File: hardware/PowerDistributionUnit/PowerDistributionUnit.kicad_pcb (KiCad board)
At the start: 2 copper layers, 99.1 x 60.2 mm, 100 parts, among them J1 973582101, J2 973582100, J3 973582101, J4 973582100, Q1 SQJ141ELP, Q2 CSD18511Q5A, SW1 SW_Push, U1 TPS25983, U2 AD5258, U3 NUCLEO_L432KC

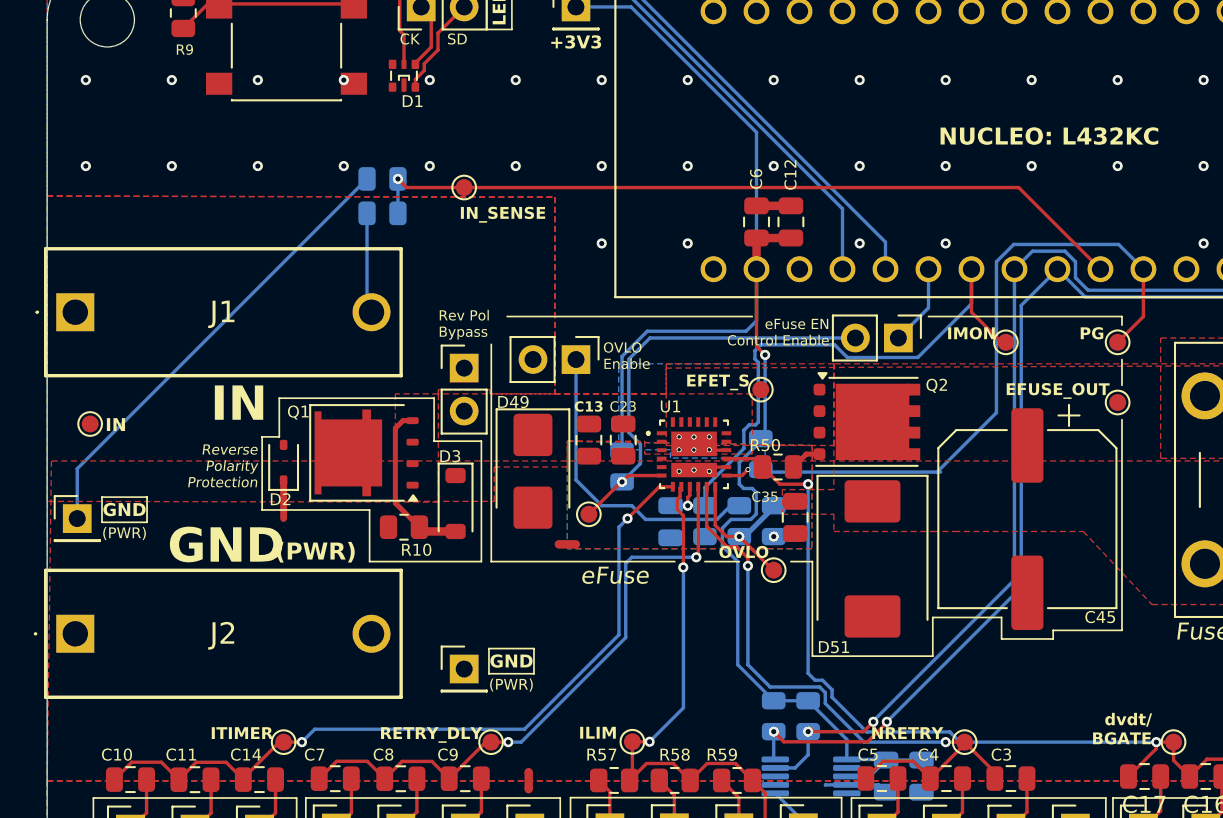
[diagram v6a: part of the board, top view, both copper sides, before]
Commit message: Changed a gnd pwr tp to gnd. Reduced capacitor value at output. Changed pwr gnd to gnd for input resistor divider.
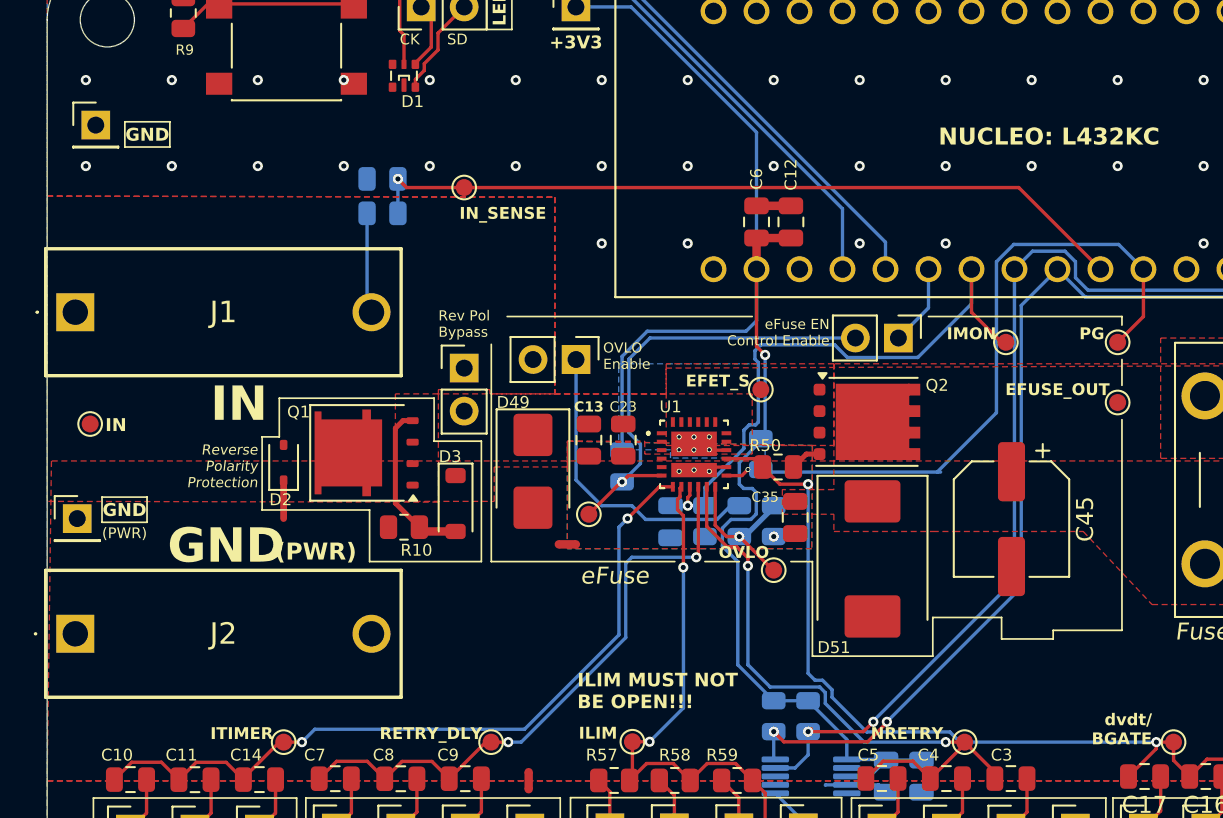
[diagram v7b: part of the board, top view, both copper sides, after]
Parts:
- C45: value 220u -> 100u; footprint Capacitor_SMD:CP_Elec_10x12.6 -> Capacitor_SMD:CP_Elec_6.3x9.9
- moved TP14 38.8 mm to (93.7, 80.5)
- moved C45 0.94 mm to (147.8, 103.8)
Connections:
- R8 pad 2: GNDPWR -> GND
- TP14 pad 1: GNDPWR -> GND
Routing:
- net GNDPWR: track 29.4 -> 2.25 mm
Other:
- board text added: "ILIM MUST NOT BE OPEN!!!"
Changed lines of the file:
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@@
 	(footprint "Connector_PinHeader_2.54mm:PinHeader_1x01_P2.54mm_Vertical"
 		(layer "F.Cu")
-		(at 115.492 112.656)
+		(at 93.726 80.518)
 		(descr "Through hole straight pin header, 1x01, 2.54mm pitch, single row")
 		(tags "Through hole pin header THT 1x01 2.54mm single row")
@@
 			(layers "*.Cu" "*.Mask")
 			(remove_unused_layers no)
-			(net 18 "GNDPWR")
+			(net 1 "GND")
 			(pinfunction "1")
 			(pintype "passive")
@@
 		)
 	)
-	(footprint "Capacitor_SMD:CP_Elec_10x12.6"
+	(footprint "Capacitor_SMD:CP_Elec_6.3x9.9"
 		(layer "F.Cu")
-		(at 148.766 103.798 -90)
-		(descr "SMD capacitor, aluminum electrolytic, Panasonic F12, 10.0x12.6mm")
+		(at 147.828 103.798 -90)
+		(descr "SMD capacitor, aluminum electrolytic, Panasonic C10, 6.3x9.9mm")
 		(tags "capacitor electrolytic")
 		(property "Reference" "C45"
-			(at 5.81 -4.318 180)
+			(at 0 -4.35 -90)
 			(layer "F.SilkS")
 			(effects
 				(font
-					(size 0.7 0.7)
-					(thickness 0.1)
+					(size 1 1)
+					(thickness 0.15)
 				)
 			)
 		)
-		(property "Value" "220u"
-			(at 0 6.2 90)
+		(property "Value" "100u"
+			(at 0 4.35 -90)
 			(layer "F.Fab")
 			(effects
@@
 			)
 		)
-		(property "Footprint" "Capacitor_SMD:CP_Elec_10x12.6"
+		(property "Footprint" "Capacitor_SMD:CP_Elec_6.3x9.9"
 			(at 0 0 -90)
 			(unlocked yes)
@@
 		(attr smd)
 		(fp_line
-			(start -4.195563 5.26)
-			(end 5.26 5.26)
+			(start -2.345563 3.41)
+			(end 3.41 3.41)
 			(stroke
 				(width 0.12)
@@
 		)
 		(fp_line
-			(start 5.26 5.26)
-			(end 5.26 1.21)
+			(start 3.41 3.41)
+			(end 3.41 1.06)
 			(stroke
 				(width 0.12)
@@
 		)
 		(fp_line
-			(start -5.26 4.195563)
-			(end -4.195563 5.26)
+			(start -3.41 2.345563)
+			(end -2.345563 3.41)
 			(stroke
 				(width 0.12)
@@
 		)
 		(fp_line
-			(start -5.26 4.195563)
-			(end -5.26 1.21)
+			(start -3.41 2.345563)
+			(end -3.41 1.06)
 			(stroke
 				(width 0.12)
@@
 		)
 		(fp_line
-			(start -6.75 -2.46)
-			(end -5.5 -2.46)
+			(start -4.4375 -1.8475)
+			(end -3.65 -1.8475)
 			(stroke
 				(width 0.12)
@@
 		)
 		(fp_line
-			(start -6.125 -3.085)
-			(end -6.125 -1.835)
+			(start -4.04375 -2.24125)
+			(end -4.04375 -1.45375)
 			(stroke
 				(width 0.12)
@@
 		)
 		(fp_line
-			(start -5.26 -4.195563)
-			(end -5.26 -1.21)
+			(start -3.41 -2.345563)
+			(end -3.41 -1.06)
 			(stroke
 				(width 0.12)
@@
 		)
 		(fp_line
-			(start -5.26 -4.195563)
-			(end -4.195563 -5.26)
+			(start -3.41 -2.345563)
+			(end -2.345563 -3.41)
 			(stroke
 				(width 0.12)
@@
 		)
 		(fp_line
-			(start -4.195563 -5.26)
-			(end 5.26 -5.26)
+			(start -2.345563 -3.41)
+			(end 3.41 -3.41)
 			(stroke
 				(width 0.12)
@@
 		)
 		(fp_line
-			(start 5.26 -5.26)
-			(end 5.26 -1.21)
+			(start 3.41 -3.41)
+			(end 3.41 -1.06)
 			(stroke
 				(width 0.12)
@@
 		)
 		(fp_line
-			(start -4.25 5.4)
-			(end 5.4 5.4)
+			(start -2.4 3.55)
+			(end 3.55 3.55)
 			(stroke
 				(width 0.05)
@@
 		)
 		(fp_line
-			(start -5.4 4.25)
-			(end -4.25 5.4)
+			(start -3.55 2.4)
+			(end -2.4 3.55)
 			(stroke
 				(width 0.05)
@@
 		)
 		(fp_line
-			(start -6.8 1.2)
-			(end -5.4 1.2)
+			(start -4.8 1.05)
+			(end -3.55 1.05)
 			(stroke
 				(width 0.05)
@@
 		)
 		(fp_line
-			(start -5.4 1.2)
-			(end -5.4 4.25)
+			(start -3.55 1.05)
+			(end -3.55 2.4)
 			(stroke
 				(width 0.05)
@@
 		)
 		(fp_line
-			(start 5.4 1.2)
-			(end 5.4 5.4)
+			(start 3.55 1.05)
+			(end 3.55 3.55)
 			(stroke
 				(width 0.05)
@@
 		)
 		(fp_line
-			(start 6.8 1.2)
-			(end 5.4 1.2)
+			(start 4.8 1.05)
+			(end 3.55 1.05)
 			(stroke
 				(width 0.05)
@@
 		)
 		(fp_line
-			(start -6.8 -1.2)
-			(end -6.8 1.2)
+			(start -4.8 -1.05)
+			(end -4.8 1.05)
 			(stroke
 				(width 0.05)
@@
 		)
 		(fp_line
-			(start -5.4 -1.2)
-			(end -6.8 -1.2)
+			(start -3.55 -1.05)
+			(end -4.8 -1.05)
 			(stroke
 				(width 0.05)
@@
 		)
 		(fp_line
-			(start 5.4 -1.2)
-			(end 6.8 -1.2)
+			(start 3.55 -1.05)
+			(end 4.8 -1.05)
 			(stroke
 				(width 0.05)
@@
 		)
 		(fp_line
-			(start 6.8 -1.2)
-			(end 6.8 1.2)
+			(start 4.8 -1.05)
+			(end 4.8 1.05)
 			(stroke
 				(width 0.05)
@@
 		)
 		(fp_line
-			(start -5.4 -4.25)
-			(end -5.4 -1.2)
+			(start -3.55 -2.4)
+			(end -3.55 -1.05)
 			(stroke
 				(width 0.05)
@@
 		)
 		(fp_line
-			(start -5.4 -4.25)
-			(end -4.25 -5.4)
+			(start -3.55 -2.4)
+			(end -2.4 -3.55)
 			(stroke
 				(width 0.05)
@@
 		)
 		(fp_line
-			(start -4.25 -5.4)
-			(end 5.4 -5.4)
+			(start -2.4 -3.55)
+			(end 3.55 -3.55)
 			(stroke
 				(width 0.05)
@@
 		)
 		(fp_line
-			(start 5.4 -5.4)
-			(end 5.4 -1.2)
+			(start 3.55 -3.55)
+			(end 3.55 -1.05)
 			(stroke
 				(width 0.05)
@@
 		)
 		(fp_line
-			(start -4.15 5.15)
-			(end 5.15 5.15)
+			(start -2.3 3.3)
+			(end 3.3 3.3)
 			(stroke
 				(width 0.1)
@@
 		)
 		(fp_line
-			(start -5.15 4.15)
-			(end -4.15 5.15)
+			(start -3.3 2.3)
+			(end -2.3 3.3)
 			(stroke
 				(width 0.1)
@@
 		)
 		(fp_line
-			(start -4.558325 -1.7)
-			(end -3.558325 -1.7)
+			(start -2.704838 -1.33)
+			(end -2.074838 -1.33)
 			(stroke
 				(width 0.1)
@@
 		)
 		(fp_line
-			(start -4.058325 -2.2)
-			(end -4.058325 -1.2)
+			(start -2.389838 -1.645)
+			(end -2.389838 -1.015)
 			(stroke
 				(width 0.1)
@@
 		)
 		(fp_line
-			(start -5.15 -4.15)
-			(end -5.15 4.15)
+			(start -3.3 -2.3)
+			(end -3.3 2.3)
 			(stroke
 				(width 0.1)
@@
 		)
 		(fp_line
-			(start -5.15 -4.15)
-			(end -4.15 -5.15)
+			(start -3.3 -2.3)
+			(end -2.3 -3.3)
 			(stroke
 				(width 0.1)
@@
 		)
 		(fp_line
-			(start -4.15 -5.15)
-			(end 5.15 -5.15)
+			(start -2.3 -3.3)
+			(end 3.3 -3.3)
 			(stroke
 				(width 0.1)
@@
 		)
 		(fp_line
-			(start 5.15 -5.15)
-			(end 5.15 5.15)
+			(start 3.3 -3.3)
+			(end 3.3 3.3)
 			(stroke
 				(width 0.1)
@@
 		(fp_circle
 			(center 0 0)
-			(end 5 0)
+			(end 3.15 0)
 			(stroke
 				(width 0.1)
@@
 		)
 		(fp_text user "${REFERENCE}"
-			(at 0 0 90)
+			(at 0 0 -90)
 			(layer "F.Fab")
 			(effects
@@
 		)
 		(pad "1" smd roundrect
-			(at -4.35 0 270)
-			(size 4.4 1.9)
+			(at -2.8 0 270)
+			(size 3.5 1.6)
 			(layers "F.Cu" "F.Paste" "F.Mask")
-			(roundrect_rratio 0.131579)
+			(roundrect_rratio 0.15625)
 			(net 17 "/EFUSE_OUT")
 			(pintype "passive")
 		)
 		(pad "2" smd roundrect
-			(at 4.35 0 270)
-			(size 4.4 1.9)
+			(at 2.8 0 270)
+			(size 3.5 1.6)
 			(layers "F.Cu" "F.Paste" "F.Mask")
-			(roundrect_rratio 0.131579)
+			(roundrect_rratio 0.15625)
 			(net 18 "GNDPWR")
 			(pintype "passive")
 		)
-		(model "${KICAD8_3DMODEL_DIR}/Capacitor_SMD.3dshapes/CP_Elec_10x12.6.wrl"
+		(model "${KICAD8_3DMODEL_DIR}/Capacitor_SMD.3dshapes/CP_Elec_6.3x9.9.wrl"
 			(offset
 				(xyz 0 0 0)
@@
 			(layers "B.Cu" "B.Paste" "B.Mask")
 			(roundrect_rratio 0.243902)
-			(net 18 "GNDPWR")
+			(net 1 "GND")
 			(pintype "passive")
 		)
@@
 	)
 	(gr_rect
-		(start 116.956 111.446)
-		(end 119.616 112.9354)
+		(start 95.444 80.324)
+		(end 98.104 81.8134)
 		(stroke
 			(width 0.1)
@@
 		)
 	)
-	(gr_text "(PWR)"
-		(at 118.286 113.9514 0)
-		(layer "F.SilkS")
-		(effects
-			(font
-				(size 0.635 0.635)
-				(thickness 0.09525)
-			)
-			(justify bottom)
-		)
-	)
 	(gr_text "IN_SENSE"
 		(at 117.778 85.732 0)
@@
 	)
 	(gr_text "GND"
-		(at 118.286 112.656 0)
+		(at 96.774 81.534 0)
 		(layer "F.SilkS" knockout)
 		(effects
@@
 		)
 	)
+	(gr_text "ILIM MUST NOT\nBE OPEN!!!"
+		(at 122.174 115.062 0)
+		(layer "F.SilkS")
+		(effects
+			(font
+				(size 0.8 0.8)
+				(thickness 0.15)
+				(bold yes)
+			)
+			(justify left bottom)
+		)
+	)
 	(gr_text "GND"
 		(at 95.426 103.706 0)
@@
 		(net 18)
 	)
-	(segment
-		(start 109.7535 83.7)
-		(end 92.632 100.8215)
-		(width 0.2)
-		(layer "B.Cu")
-		(net 18)
-	)
-	(segment
-		(start 92.632 100.8215)
-		(end 92.632 103.766)
-		(width 0.2)
-		(layer "B.Cu")
-		(net 18)
-	)

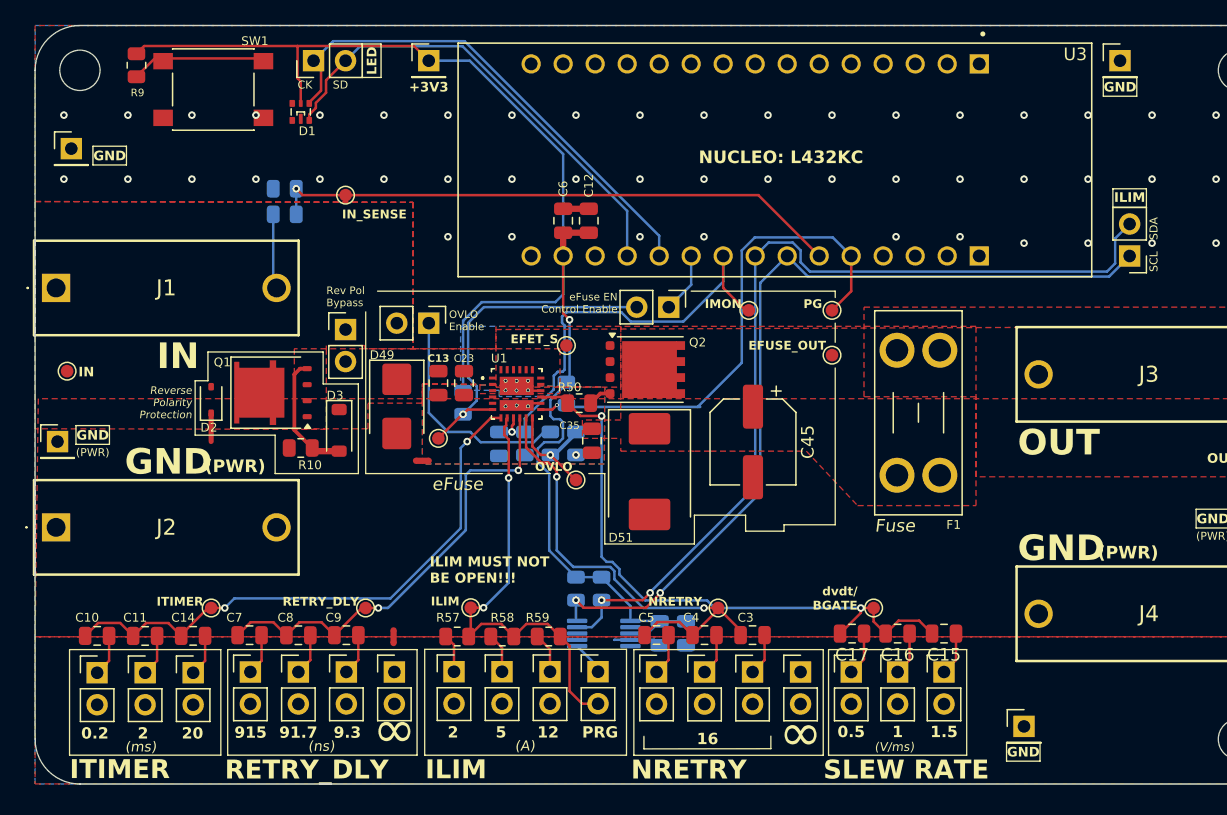
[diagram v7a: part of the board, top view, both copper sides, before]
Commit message: Resolved all DRC errors.
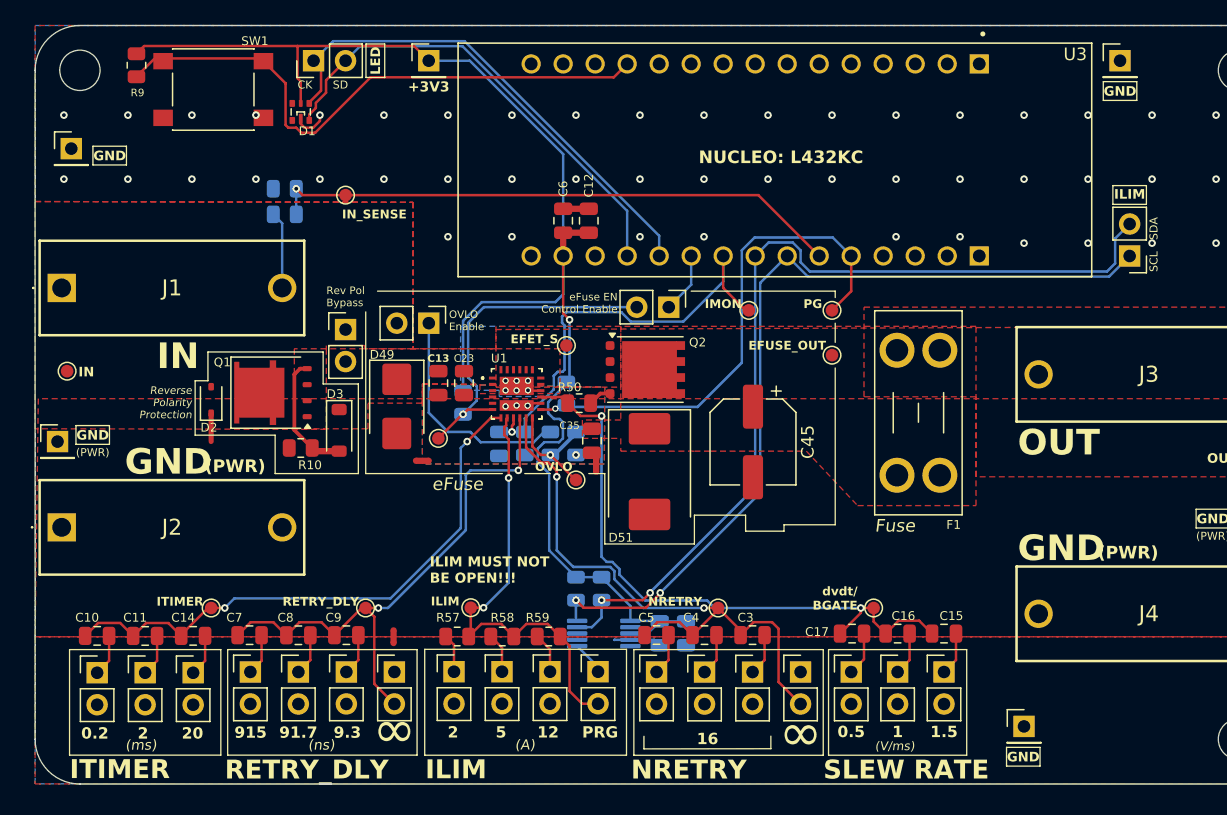
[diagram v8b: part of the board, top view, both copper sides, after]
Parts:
- added NT3: NetTie_2, NetTie:NetTie-2_SMD_Pad0.5mm, F.Cu at (135.4, 105.7)
- moved J1 0.45 mm to (93.0, 91.6)
- moved J2 0.45 mm to (93.0, 110.6)
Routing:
- net /IND_BTN: track 11.3 -> 46.7 mm
- net /NRETRY: track 37.5 -> 47.8 mm
- net /RETRY_DLY: track 36.3 -> 44.8 mm
- net GND: track 7.79 -> 10.5 mm
